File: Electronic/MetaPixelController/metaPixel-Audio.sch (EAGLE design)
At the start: 2 parts

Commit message: procrastinating - minor changes to the Audio version -
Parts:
- added IC1: 74HC245N, 74xx-eu:74HC245N
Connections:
- new net DMX_IN_3V: U$1.0
- new net N$1: IC1A.A2
- new net N$2: IC1A.A3
- new net WS2812D: IC1A.A1, U$1.4
- new net WS2812O: IC1A.B1
- net !ADS_CS: now also U$1.21/A7
- net !LCD_CS: now also U$1.20/A6
- net !LCD_RST: now also U$1.2
- net GND: now also IC1A.G
- net LCD_LED: now also U$1.3
- net VCC: now also IC1A.DIR
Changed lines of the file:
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@@
 <part name="P+2" library="supply1" deviceset="VCC" device=""/>
 <part name="SV1" library="con-harting-ml" deviceset="ML14" device=""/>
+<part name="IC1" library="74xx-eu" deviceset="74*245" device="N" technology="HC"/>
+<part name="P+3" library="supply1" deviceset="VCC" device=""/>
+<part name="GND2" library="supply1" deviceset="GND" device=""/>
 </parts>
 <sheets>
@@
 <instance part="P+2" gate="VCC" x="68.58" y="58.42" rot="R270"/>
 <instance part="SV1" gate="1" x="142.24" y="40.64"/>
+<instance part="IC1" gate="A" x="96.52" y="-27.94"/>
+<instance part="P+3" gate="VCC" x="68.58" y="-38.1" rot="R90"/>
+<instance part="GND2" gate="1" x="71.12" y="-43.18"/>
 </instances>
 <busses>
@@
 <pinref part="SV1" gate="1" pin="2"/>
 </segment>
+<segment>
+<pinref part="IC1" gate="A" pin="G"/>
+<wire x1="83.82" y1="-40.64" x2="71.12" y2="-40.64" width="0.1524" layer="91"/>
+<pinref part="GND2" gate="1" pin="GND"/>
+</segment>
 </net>
 <net name="VCC" class="0">
@@
 <pinref part="P+2" gate="VCC" pin="VCC"/>
 </segment>
+<segment>
+<pinref part="IC1" gate="A" pin="DIR"/>
+<wire x1="83.82" y1="-38.1" x2="71.12" y2="-38.1" width="0.1524" layer="91"/>
+<pinref part="P+3" gate="VCC" pin="VCC"/>
+</segment>
 </net>
 <net name="LCD_LED" class="0">
@@
 <pinref part="SV1" gate="1" pin="5"/>
 </segment>
+<segment>
+<pinref part="U$1" gate="G$1" pin="3"/>
+<wire x1="22.86" y1="48.26" x2="10.16" y2="48.26" width="0.1524" layer="91"/>
+<label x="10.16" y="48.26" size="1.4224" layer="95"/>
+</segment>
 </net>
 <net name="!LCD_CS" class="0">
@@
 <pinref part="SV1" gate="1" pin="7"/>
 </segment>
+<segment>
+<pinref part="U$1" gate="G$1" pin="20/A6"/>
+<wire x1="53.34" y1="38.1" x2="66.04" y2="38.1" width="0.1524" layer="91"/>
+<label x="55.88" y="38.1" size="1.4224" layer="95"/>
+</segment>
 </net>
 <net name="!LCD_RST" class="0">
@@
 <pinref part="SV1" gate="1" pin="6"/>
 </segment>
+<segment>
+<pinref part="U$1" gate="G$1" pin="2"/>
+<wire x1="22.86" y1="50.8" x2="10.16" y2="50.8" width="0.1524" layer="91"/>
+<label x="10.16" y="50.8" size="1.4224" layer="95"/>
+</segment>
 </net>
 <net name="!ADS_CS" class="0">
@@
 <pinref part="SV1" gate="1" pin="11"/>
 </segment>
-</net>
+<segment>
+<pinref part="U$1" gate="G$1" pin="21/A7"/>
+<wire x1="53.34" y1="40.64" x2="66.04" y2="40.64" width="0.1524" layer="91"/>
+<label x="55.88" y="40.64" size="1.4224" layer="95"/>
+</segment>
+</net>
+<net name="DMX_IN_3V" class="0">
+<segment>
+<pinref part="U$1" gate="G$1" pin="0"/>
+<wire x1="22.86" y1="55.88" x2="10.16" y2="55.88" width="0.1524" layer="91"/>
+<label x="10.16" y="55.88" size="1.4224" layer="95"/>
+</segment>
+</net>
+<net name="WS2812D" class="0">
+<segment>
+<pinref part="U$1" gate="G$1" pin="4"/>
+<wire x1="22.86" y1="45.72" x2="10.16" y2="45.72" width="0.1524" layer="91"/>
+<label x="10.16" y="45.72" size="1.4224" layer="95"/>
+</segment>
+<segment>
+<pinref part="IC1" gate="A" pin="A1"/>
+<wire x1="83.82" y1="-15.24" x2="68.58" y2="-15.24" width="0.1524" layer="91"/>
+<label x="68.58" y="-15.24" size="1.778" layer="95"/>
+</segment>
+</net>
+<net name="WS2812O" class="0">
+<segment>
+<pinref part="IC1" gate="A" pin="B1"/>
+<wire x1="109.22" y1="-15.24" x2="124.46" y2="-15.24" width="0.1524" layer="91"/>
+<label x="114.3" y="-15.24" size="1.778" layer="95"/>
+</segment>
+</net>
+<net name="N$1" class="0">
+<segment>
+<pinref part="IC1" gate="A" pin="A2"/>
+<wire x1="83.82" y1="-17.78" x2="68.58" y2="-17.78" width="0.1524" layer="91"/>
+</segment>
+</net>
+<net name="N$2" class="0">
+<segment>
+<pinref part="IC1" gate="A" pin="A3"/>
+<wire x1="83.82" y1="-20.32" x2="68.58" y2="-20.32" width="0.1524" layer="91"/>
+</segment>
+</net>

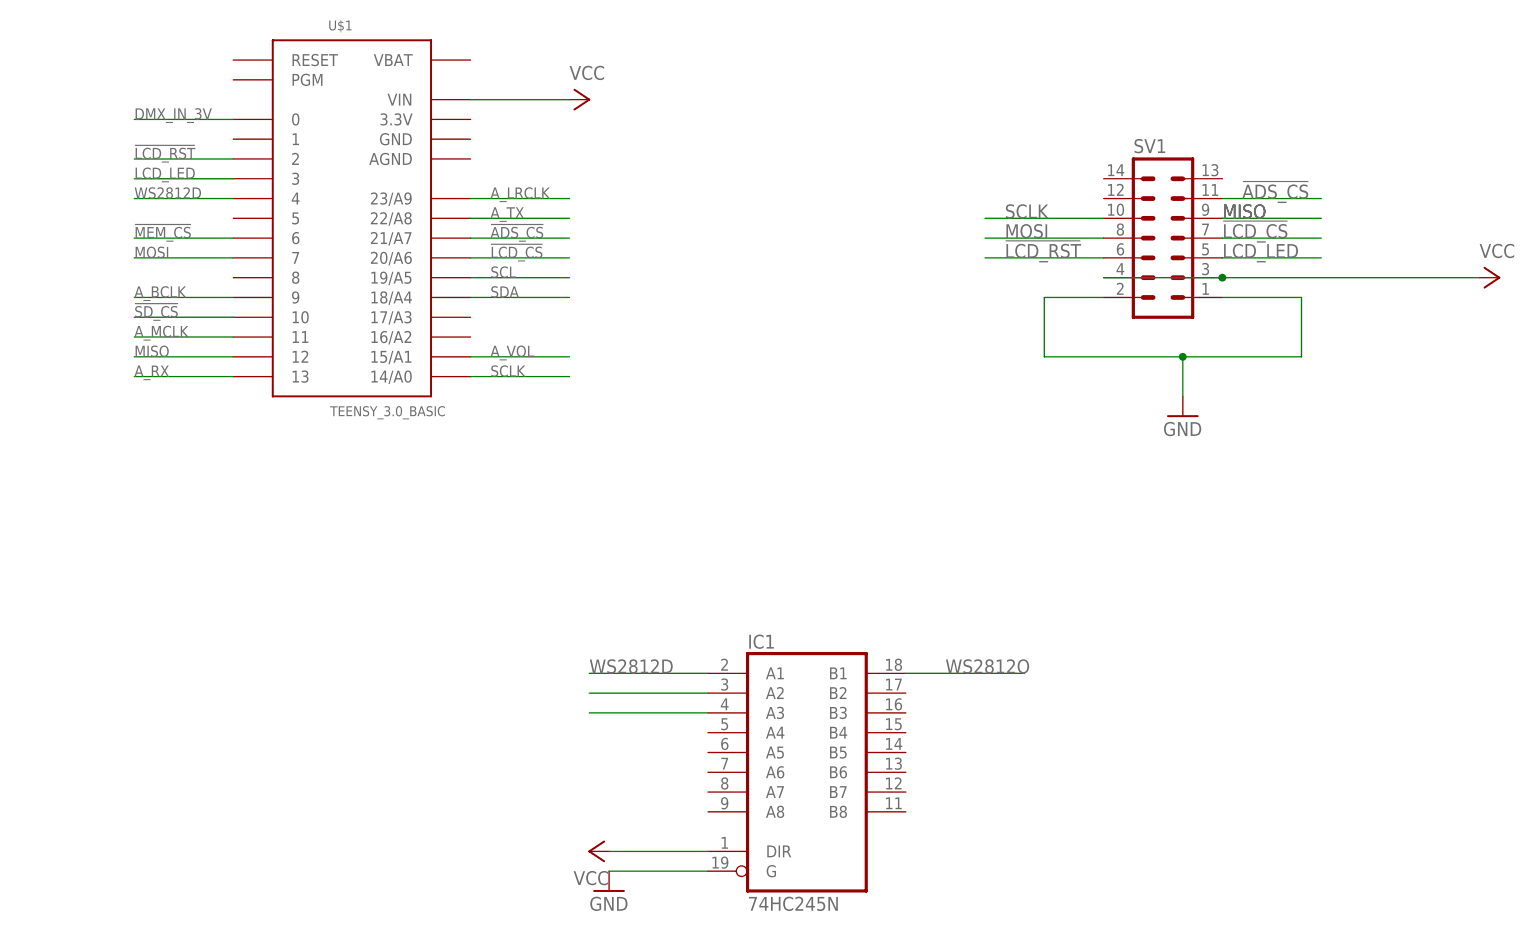
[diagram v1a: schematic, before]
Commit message: Stuff
resolution switch for display
renaming of globals
output of parameter settings adapts automatically to new parameters
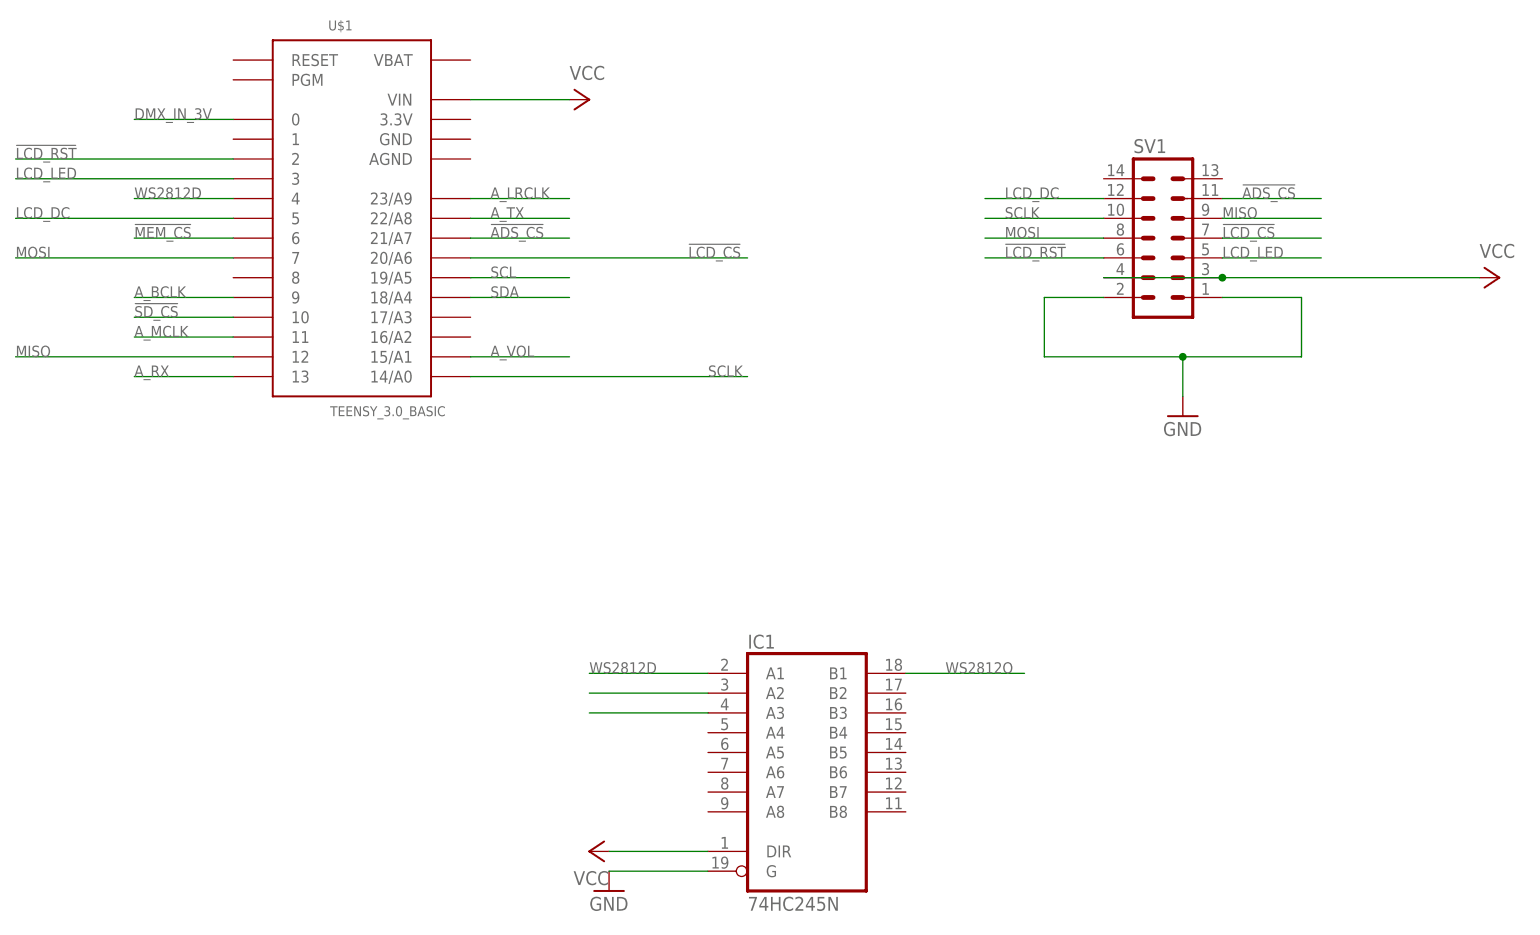
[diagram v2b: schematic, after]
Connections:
- new net LCD_DC: SV1.12, U$1.5
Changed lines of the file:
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@@
 <segment>
 <pinref part="U$1" gate="G$1" pin="14/A0"/>
-<wire x1="53.34" y1="22.86" x2="66.04" y2="22.86" width="0.1524" layer="91"/>
-<label x="55.88" y="22.86" size="1.4224" layer="95"/>
+<wire x1="53.34" y1="22.86" x2="88.9" y2="22.86" width="0.1524" layer="91"/>
+<label x="83.82" y="22.86" size="1.4224" layer="95"/>
 </segment>
 <segment>
 <wire x1="134.62" y1="43.18" x2="119.38" y2="43.18" width="0.1524" layer="91"/>
-<label x="121.92" y="43.18" size="1.778" layer="95"/>
+<label x="121.92" y="43.18" size="1.4224" layer="95"/>
 <pinref part="SV1" gate="1" pin="10"/>
 </segment>
@@
 <segment>
 <pinref part="U$1" gate="G$1" pin="7"/>
-<wire x1="22.86" y1="38.1" x2="10.16" y2="38.1" width="0.1524" layer="91"/>
-<label x="10.16" y="38.1" size="1.4224" layer="95"/>
+<wire x1="22.86" y1="38.1" x2="-5.08" y2="38.1" width="0.1524" layer="91"/>
+<label x="-5.08" y="38.1" size="1.4224" layer="95"/>
 </segment>
 <segment>
 <wire x1="134.62" y1="40.64" x2="119.38" y2="40.64" width="0.1524" layer="91"/>
-<label x="121.92" y="40.64" size="1.778" layer="95"/>
+<label x="121.92" y="40.64" size="1.4224" layer="95"/>
 <pinref part="SV1" gate="1" pin="8"/>
 </segment>
@@
 <segment>
 <pinref part="U$1" gate="G$1" pin="12"/>
-<wire x1="22.86" y1="25.4" x2="10.16" y2="25.4" width="0.1524" layer="91"/>
-<label x="10.16" y="25.4" size="1.4224" layer="95"/>
+<wire x1="22.86" y1="25.4" x2="-5.08" y2="25.4" width="0.1524" layer="91"/>
+<label x="-5.08" y="25.4" size="1.4224" layer="95"/>
 </segment>
 <segment>
 <wire x1="149.86" y1="43.18" x2="162.56" y2="43.18" width="0.1524" layer="91"/>
-<label x="149.86" y="43.18" size="1.778" layer="95"/>
-<label x="149.86" y="43.18" size="1.778" layer="95"/>
+<label x="149.86" y="43.18" size="1.4224" layer="95"/>
 <pinref part="SV1" gate="1" pin="9"/>
 </segment>
@@
 <segment>
 <wire x1="149.86" y1="38.1" x2="162.56" y2="38.1" width="0.1524" layer="91"/>
-<label x="149.86" y="38.1" size="1.778" layer="95"/>
+<label x="149.86" y="38.1" size="1.4224" layer="95"/>
 <pinref part="SV1" gate="1" pin="5"/>
 </segment>
 <segment>
 <pinref part="U$1" gate="G$1" pin="3"/>
-<wire x1="22.86" y1="48.26" x2="10.16" y2="48.26" width="0.1524" layer="91"/>
-<label x="10.16" y="48.26" size="1.4224" layer="95"/>
+<wire x1="22.86" y1="48.26" x2="-5.08" y2="48.26" width="0.1524" layer="91"/>
+<label x="-5.08" y="48.26" size="1.4224" layer="95"/>
 </segment>
 </net>
@@
 <segment>
 <wire x1="149.86" y1="40.64" x2="162.56" y2="40.64" width="0.1524" layer="91"/>
-<label x="149.86" y="40.64" size="1.778" layer="95"/>
+<label x="149.86" y="40.64" size="1.4224" layer="95"/>
 <pinref part="SV1" gate="1" pin="7"/>
 </segment>
 <segment>
 <pinref part="U$1" gate="G$1" pin="20/A6"/>
-<wire x1="53.34" y1="38.1" x2="66.04" y2="38.1" width="0.1524" layer="91"/>
-<label x="55.88" y="38.1" size="1.4224" layer="95"/>
+<wire x1="53.34" y1="38.1" x2="88.9" y2="38.1" width="0.1524" layer="91"/>
+<label x="81.28" y="38.1" size="1.4224" layer="95"/>
 </segment>
 </net>
@@
 <segment>
 <wire x1="134.62" y1="38.1" x2="119.38" y2="38.1" width="0.1524" layer="91"/>
-<label x="121.92" y="38.1" size="1.778" layer="95"/>
+<label x="121.92" y="38.1" size="1.4224" layer="95"/>
 <pinref part="SV1" gate="1" pin="6"/>
 </segment>
 <segment>
 <pinref part="U$1" gate="G$1" pin="2"/>
-<wire x1="22.86" y1="50.8" x2="10.16" y2="50.8" width="0.1524" layer="91"/>
-<label x="10.16" y="50.8" size="1.4224" layer="95"/>
+<wire x1="22.86" y1="50.8" x2="-5.08" y2="50.8" width="0.1524" layer="91"/>
+<label x="-5.08" y="50.8" size="1.4224" layer="95"/>
 </segment>
 </net>
@@
 <segment>
 <wire x1="149.86" y1="45.72" x2="162.56" y2="45.72" width="0.1524" layer="91"/>
-<label x="152.4" y="45.72" size="1.778" layer="95"/>
+<label x="152.4" y="45.72" size="1.4224" layer="95"/>
 <pinref part="SV1" gate="1" pin="11"/>
 </segment>
@@
 <pinref part="IC1" gate="A" pin="A1"/>
 <wire x1="83.82" y1="-15.24" x2="68.58" y2="-15.24" width="0.1524" layer="91"/>
-<label x="68.58" y="-15.24" size="1.778" layer="95"/>
+<label x="68.58" y="-15.24" size="1.4224" layer="95"/>
 </segment>
 </net>
@@
 <pinref part="IC1" gate="A" pin="B1"/>
 <wire x1="109.22" y1="-15.24" x2="124.46" y2="-15.24" width="0.1524" layer="91"/>
-<label x="114.3" y="-15.24" size="1.778" layer="95"/>
+<label x="114.3" y="-15.24" size="1.4224" layer="95"/>
 </segment>
 </net>
@@
 </segment>
 </net>
+<net name="LCD_DC" class="0">
+<segment>
+<pinref part="SV1" gate="1" pin="12"/>
+<wire x1="134.62" y1="45.72" x2="119.38" y2="45.72" width="0.1524" layer="91"/>
+<label x="121.92" y="45.72" size="1.4224" layer="95"/>
+</segment>
+<segment>
+<pinref part="U$1" gate="G$1" pin="5"/>
+<wire x1="22.86" y1="43.18" x2="-5.08" y2="43.18" width="0.1524" layer="91"/>
+<label x="-5.08" y="43.18" size="1.4224" layer="95"/>
+</segment>
+</net>
